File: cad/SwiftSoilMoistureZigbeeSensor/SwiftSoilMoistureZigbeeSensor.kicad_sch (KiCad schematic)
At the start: 13 parts, among them J1 Probe, J2 BAT, J3 ARM SWD 10, Q1 BSS84, SW1 Factory Reset, U1 TPS61221DCK, U2 E73-2G4M08S1C

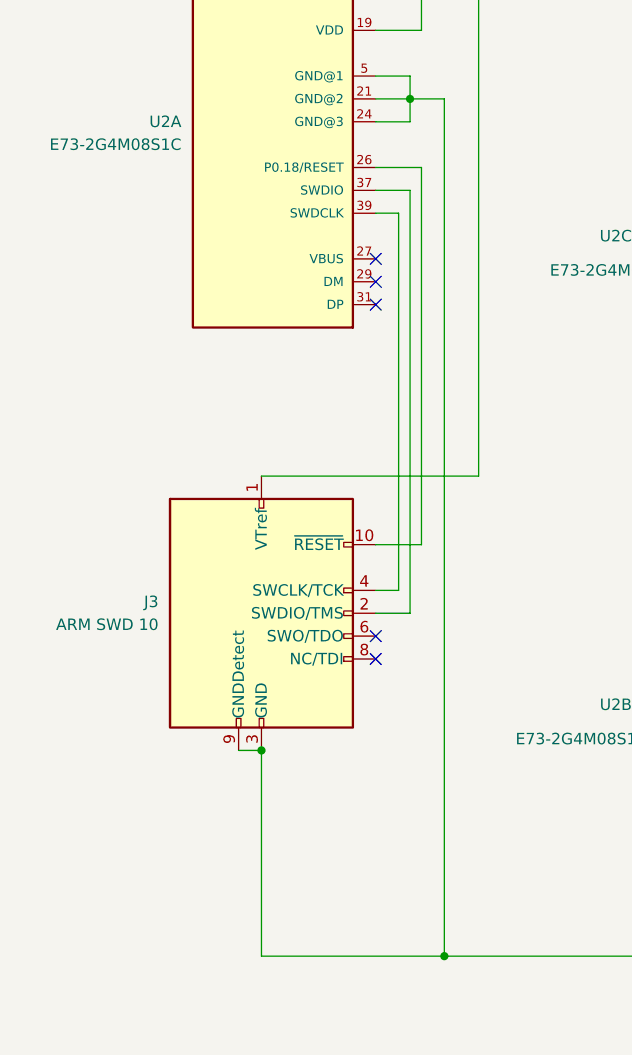
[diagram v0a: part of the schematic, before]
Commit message: Changed SWD connector
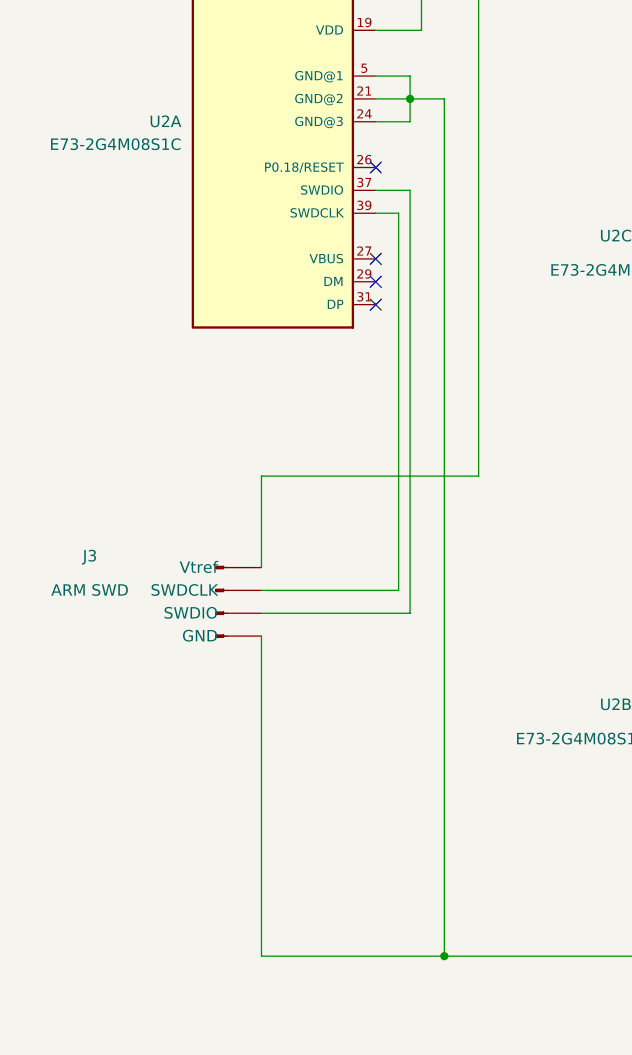
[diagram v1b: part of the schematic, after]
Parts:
- J3: value ARM SWD 10 -> ARM SWD; footprint Connector_PinHeader_1.27mm:PinHeader_2x05_P1.27mm_Vertical_SMD -> Connector_PinHeader_2.54mm:PinHeader_1x04_P2.54mm_Vertical; symbol Connector:Conn_ARM_JTAG_SWD_10 -> Connector:Conn_01x04_Pin; LCSC C2932107 -> (none)
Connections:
- net GND: now also J3.4 (GND); no longer J3.3 (GND), J3.5 (GND), J3.9 (GNDDetect)
- net at U2.26 (P0.18/RESET): no longer J3.10 (~{RESET})
- net at U2.37 (SWDIO): now also J3.3 (SWDIO); no longer J3.2 (SWDIO/TMS)
- net at U2.39 (SWDCLK): now also J3.2 (SWDCLK); no longer J3.4 (SWCLK/TCK)
- no-connect marks 32 -> 31
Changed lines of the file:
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@@
   (junction (at 171.45 60.96) (diameter 0) (color 0 0 0 0)
-  )
-  (junction (at 52.07 120.65) (diameter 0) (color 0 0 0 0)
   )
   (junction (at 130.81 143.51) (diameter 0) (color 0 0 0 0)
@@
   (no_connect (at 64.77 35.56))
   (no_connect (at 114.3 116.84))
+  (no_connect (at 64.77 55.88))
   (no_connect (at 114.3 81.28))
-  (no_connect (at 64.77 110.49))
   (no_connect (at 114.3 104.14))
   (no_connect (at 114.3 132.08))
@@
   (no_connect (at 114.3 96.52))
   (no_connect (at 114.3 57.15))
-  (no_connect (at 64.77 107.95))
   (no_connect (at 114.3 64.77))
   (no_connect (at 114.3 114.3))
@@
   (no_connect (at 114.3 99.06))
   (no_connect (at 114.3 134.62))
-  (wire (pts (xy 52.07 120.65) (xy 49.53 120.65))
-    (stroke (width 0) (type default))
-  )
   (wire (pts (xy 72.39 48.26) (xy 72.39 143.51))
     (stroke (width 0) (type default))
@@
     (stroke (width 0) (type default))
   )
-  (wire (pts (xy 64.77 102.87) (xy 67.31 102.87))
-    (stroke (width 0) (type default))
-  )
   (wire (pts (xy 114.3 88.9) (xy 179.07 88.9))
     (stroke (width 0) (type default))
@@
     (stroke (width 0) (type default))
   )
-  (wire (pts (xy 64.77 105.41) (xy 68.58 105.41))
+  (wire (pts (xy 52.07 105.41) (xy 68.58 105.41))
     (stroke (width 0) (type default))
   )
@@
     (stroke (width 0) (type default))
   )
-  (wire (pts (xy 69.85 55.88) (xy 69.85 97.79))
-    (stroke (width 0) (type default))
-  )
   (wire (pts (xy 179.07 49.53) (xy 181.61 49.53))
     (stroke (width 0) (type default))
   )
-  (wire (pts (xy 52.07 120.65) (xy 52.07 143.51))
-    (stroke (width 0) (type default))
-  )
   (wire (pts (xy 171.45 49.53) (xy 171.45 52.07))
     (stroke (width 0) (type default))
   )
+  (wire (pts (xy 52.07 102.87) (xy 67.31 102.87))
+    (stroke (width 0) (type default))
+  )
   (wire (pts (xy 227.33 88.9) (xy 241.3 88.9))
     (stroke (width 0) (type default))
@@
     (stroke (width 0) (type default))
   )
-  (wire (pts (xy 69.85 55.88) (xy 64.77 55.88))
-    (stroke (width 0) (type default))
-  )
   (wire (pts (xy 64.77 40.64) (xy 69.85 40.64))
     (stroke (width 0) (type default))
@@
     (stroke (width 0) (type default))
   )
+  (wire (pts (xy 52.07 107.95) (xy 52.07 143.51))
+    (stroke (width 0) (type default))
+  )
   (wire (pts (xy 68.58 48.26) (xy 72.39 48.26))
     (stroke (width 0) (type default))
@@
     (stroke (width 0) (type default))
   )
+  (wire (pts (xy 52.07 90.17) (xy 52.07 100.33))
+    (stroke (width 0) (type default))
+  )
   (wire (pts (xy 64.77 50.8) (xy 68.58 50.8))
     (stroke (width 0) (type default))
@@
   )
   (wire (pts (xy 179.07 52.07) (xy 179.07 88.9))
-    (stroke (width 0) (type default))
-  )
-  (wire (pts (xy 64.77 97.79) (xy 69.85 97.79))
     (stroke (width 0) (type default))
   )
@@
     )
   )
-  (symbol (lib_id "Connector:Conn_ARM_JTAG_SWD_10") (at 52.07 105.41 0) (unit 1)
-    (in_bom yes) (on_board yes) (dnp no) (fields_autoplaced)
-    (property "Reference" "J3" (at 40.64 104.14 0)
-      (effects (font (size 1.27 1.27)) (justify right))
-    )
-    (property "Value" "ARM SWD 10" (at 40.64 106.68 0)
-      (effects (font (size 1.27 1.27)) (justify right))
-    )
-    (property "Footprint" "Connector_PinHeader_1.27mm:PinHeader_2x05_P1.27mm_Vertical_SMD" (at 52.07 105.41 0)
-      (effects (font (size 1.27 1.27)) hide)
-    )
-    (property "Datasheet" "http://infocenter.arm.com/help/topic/com.arm.doc.ddi0314h/DDI0314H_coresight_components_trm.pdf" (at 43.18 137.16 90)
-      (effects (font (size 1.27 1.27)) hide)
-    )
-    (property "LCSC" "C2932107" (at 52.07 105.41 0)
-      (effects (font (size 1.27 1.27)) hide)
-    )
-    (pin "5")
+  (symbol (lib_id "Connector:Conn_01x04_Pin") (at 46.99 102.87 0) (unit 1)
+    (in_bom yes) (on_board yes) (dnp no)
+    (property "Reference" "J3" (at 33.02 99.06 0)
+      (effects (font (size 1.27 1.27)))
+    )
+    (property "Value" "ARM SWD" (at 33.02 102.87 0)
+      (effects (font (size 1.27 1.27)))
+    )
+    (property "Footprint" "Connector_PinHeader_2.54mm:PinHeader_1x04_P2.54mm_Vertical" (at 46.99 96.52 0)
+      (effects (font (size 1.27 1.27)) hide)
+    )
+    (property "Datasheet" "~" (at 46.99 102.87 0)
+      (effects (font (size 1.27 1.27)) hide)
+    )
+    (property "LCSC" "" (at 46.99 102.87 0)
+      (effects (font (size 1.27 1.27)) hide)
+    )
     (pin "2")
     (pin "3")
     (pin "4")
-    (pin "6")
-    (pin "10")
-    (pin "1")
-    (pin "7")
-    (pin "9")
-    (pin "8")
-    (instances
-      (project "SwiftSoilMoistureZigbeeSensor"
+    (pin "1")
+    (instances
+      (project "SwiftSoilMoistureZigbeeSensor"

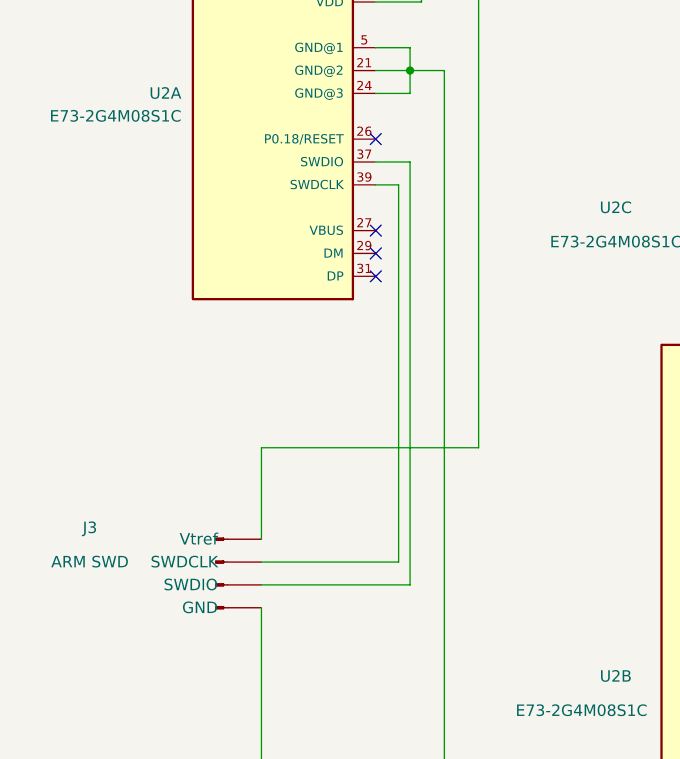
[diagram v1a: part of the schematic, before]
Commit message: Rewworked SWD connector
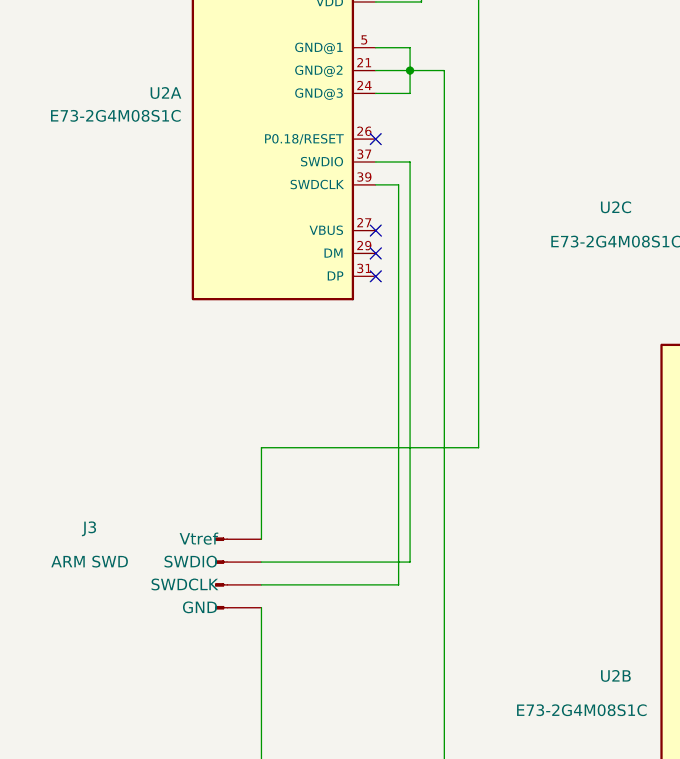
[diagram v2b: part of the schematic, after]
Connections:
- net at U2.37 (SWDIO): now also J3.2 (SWDIO); no longer J3.3 (SWDIO)
- net at U2.39 (SWDCLK): now also J3.3 (SWDCLK); no longer J3.2 (SWDCLK)
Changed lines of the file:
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@@
+    (stroke (width 0) (type default))
+  )
+  (wire (pts (xy 67.31 105.41) (xy 52.07 105.41))
     (stroke (width 0) (type default))
   )
@@
     (stroke (width 0) (type default))
   )
-  (wire (pts (xy 52.07 105.41) (xy 68.58 105.41))
+  (wire (pts (xy 196.85 60.96) (xy 208.28 60.96))
     (stroke (width 0) (type default))
   )
-  (wire (pts (xy 196.85 60.96) (xy 208.28 60.96))
+  (wire (pts (xy 52.07 102.87) (xy 68.58 102.87))
     (stroke (width 0) (type default))
   )
@@
   )
   (wire (pts (xy 171.45 49.53) (xy 171.45 52.07))
-    (stroke (width 0) (type default))
-  )
-  (wire (pts (xy 52.07 102.87) (xy 67.31 102.87))
     (stroke (width 0) (type default))
   )
@@
     (stroke (width 0) (type default))
   )
-  (wire (pts (xy 67.31 60.96) (xy 67.31 102.87))
-    (stroke (width 0) (type default))
-  )
   (wire (pts (xy 72.39 143.51) (xy 130.81 143.51))
     (stroke (width 0) (type default))
@@
   )
   (wire (pts (xy 52.07 90.17) (xy 76.2 90.17))
+    (stroke (width 0) (type default))
+  )
+  (wire (pts (xy 67.31 60.96) (xy 67.31 105.41))
     (stroke (width 0) (type default))
   )
@@
     (stroke (width 0) (type default))
   )
-  (wire (pts (xy 68.58 58.42) (xy 68.58 105.41))
+  (wire (pts (xy 68.58 58.42) (xy 68.58 102.87))
     (stroke (width 0) (type default))
   )

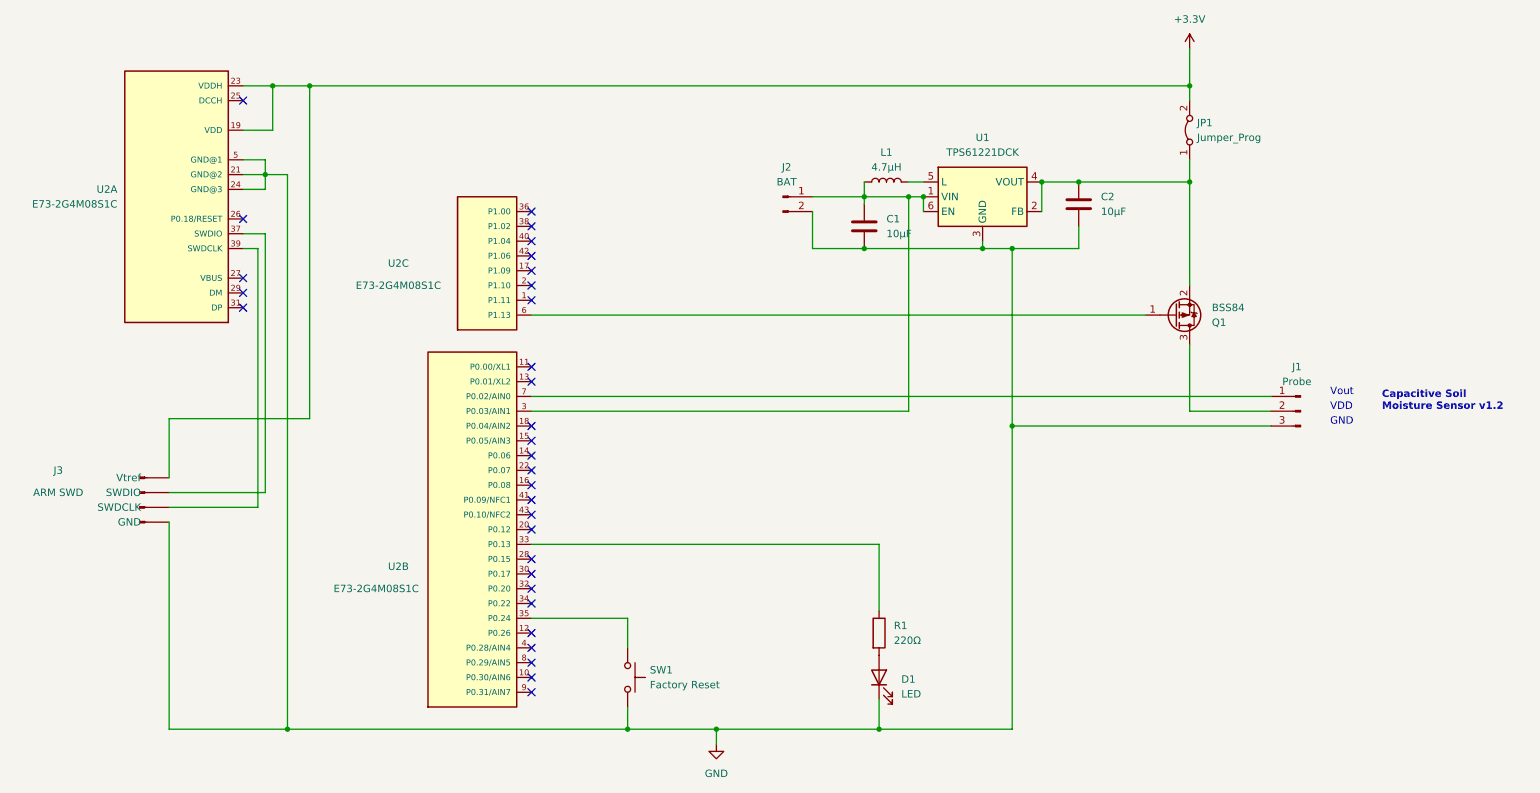
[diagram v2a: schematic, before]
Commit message: Bad LED wiring
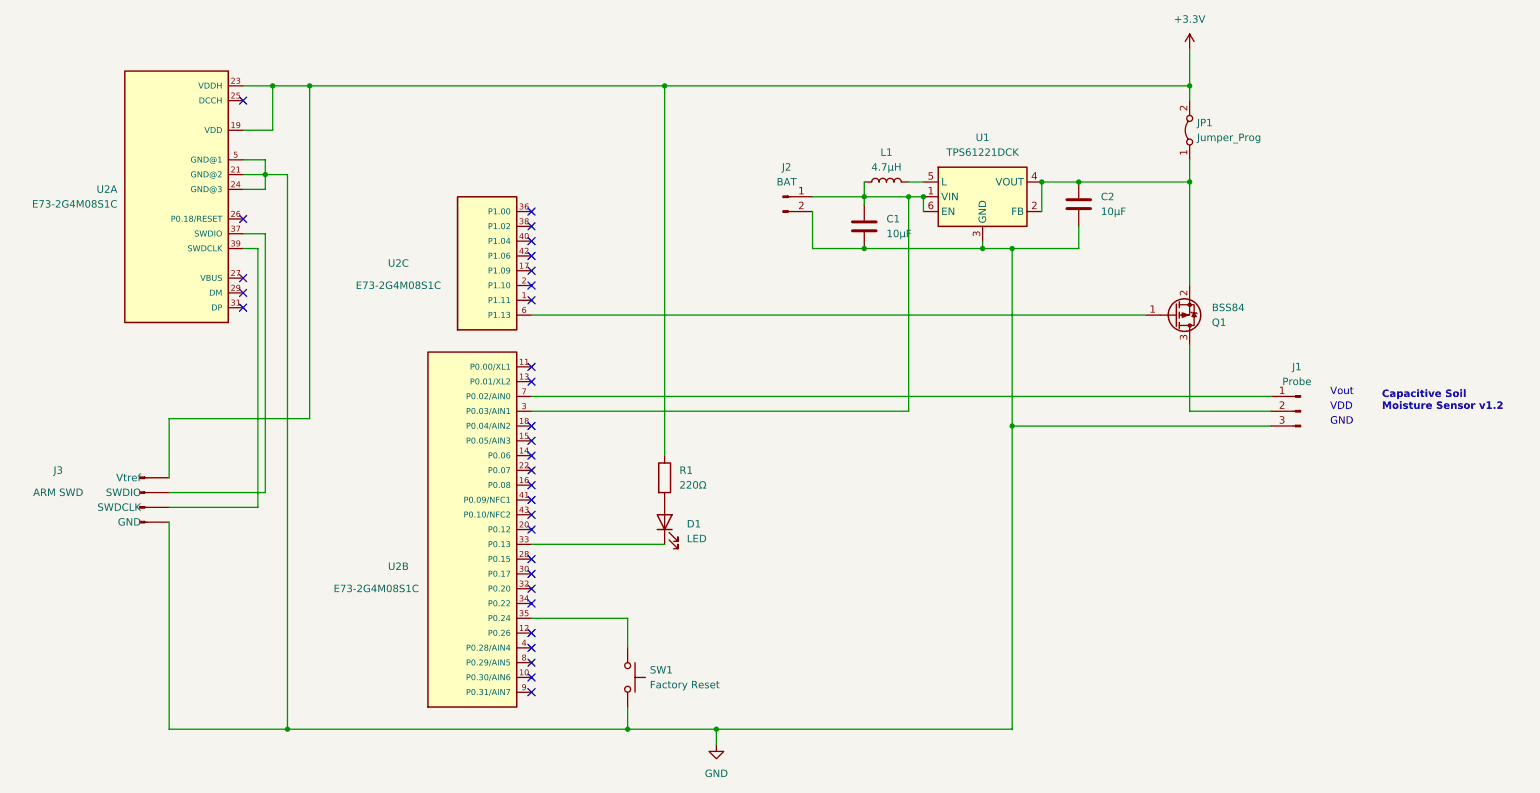
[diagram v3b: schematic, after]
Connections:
- net +3.3V: now also R1.1
- net GND: no longer D1.1 (K)
- net at U2.33 (P0.13): now also D1.1 (K); no longer R1.1
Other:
- moved on the sheet: D1, R1
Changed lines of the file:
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@@
   (title_block
     (title "Swift Zigbee Soil Moisture Sensor")
-    (date "2024-07-04")
-    (rev "1.0")
+    (date "2024-08-13")
+    (rev "1.1")
   )
   (junction (at 196.85 60.96) (diameter 0) (color 0 0 0 0)
@@
   (junction (at 208.28 49.53) (diameter 0) (color 0 0 0 0)
   )
+  (junction (at 137.16 33.02) (diameter 0) (color 0 0 0 0)
+  )
   (junction (at 179.07 52.07) (diameter 0) (color 0 0 0 0)
-  )
-  (junction (at 173.99 143.51) (diameter 0) (color 0 0 0 0)
   )
   (junction (at 191.77 60.96) (diameter 0) (color 0 0 0 0)
@@
     (stroke (width 0) (type default))
   )
-  (wire (pts (xy 173.99 138.43) (xy 173.99 143.51))
+  (wire (pts (xy 137.16 33.02) (xy 137.16 96.52))
     (stroke (width 0) (type default))
   )
@@
     (stroke (width 0) (type default))
   )
+  (wire (pts (xy 76.2 33.02) (xy 137.16 33.02))
+    (stroke (width 0) (type default))
+  )
   (wire (pts (xy 208.28 57.15) (xy 208.28 60.96))
     (stroke (width 0) (type default))
@@
     (stroke (width 0) (type default))
   )
-  (wire (pts (xy 173.99 143.51) (xy 196.85 143.51))
+  (wire (pts (xy 146.05 143.51) (xy 196.85 143.51))
     (stroke (width 0) (type default))
   )
@@
     (stroke (width 0) (type default))
   )
-  (wire (pts (xy 146.05 143.51) (xy 173.99 143.51))
-    (stroke (width 0) (type default))
-  )
   (wire (pts (xy 179.07 52.07) (xy 181.61 52.07))
     (stroke (width 0) (type default))
   )
+  (wire (pts (xy 137.16 33.02) (xy 227.33 33.02))
+    (stroke (width 0) (type default))
+  )
   (wire (pts (xy 72.39 143.51) (xy 130.81 143.51))
     (stroke (width 0) (type default))
@@
     (stroke (width 0) (type default))
   )
-  (wire (pts (xy 173.99 111.76) (xy 114.3 111.76))
+  (wire (pts (xy 137.16 111.76) (xy 114.3 111.76))
     (stroke (width 0) (type default))
   )
@@
     (stroke (width 0) (type default))
   )
-  (wire (pts (xy 173.99 123.19) (xy 173.99 111.76))
-    (stroke (width 0) (type default))
-  )
   (wire (pts (xy 52.07 143.51) (xy 72.39 143.51))
     (stroke (width 0) (type default))
@@
   )
   (wire (pts (xy 68.58 48.26) (xy 72.39 48.26))
-    (stroke (width 0) (type default))
-  )
-  (wire (pts (xy 76.2 33.02) (xy 227.33 33.02))
     (stroke (width 0) (type default))
   )
@@
     )
   )
-  (symbol (lib_id "Device:R") (at 173.99 127 0) (unit 1)
+  (symbol (lib_id "Device:R") (at 137.16 100.33 0) (unit 1)
     (in_bom yes) (on_board yes) (dnp no) (fields_autoplaced)
-    (property "Reference" "R1" (at 176.53 125.73 0)
+    (property "Reference" "R1" (at 139.7 99.06 0)
       (effects (font (size 1.27 1.27)) (justify left))
     )
-    (property "Value" "220Ω" (at 176.53 128.27 0)
+    (property "Value" "220Ω" (at 139.7 101.6 0)
       (effects (font (size 1.27 1.27)) (justify left))
     )
-    (property "Footprint" "Resistor_SMD:R_0603_1608Metric" (at 172.212 127 90)
-      (effects (font (size 1.27 1.27)) hide)
-    )
-    (property "Datasheet" "~" (at 173.99 127 0)
-      (effects (font (size 1.27 1.27)) hide)
-    )
-    (property "LCSC" "C445820" (at 173.99 127 0)
+    (property "Footprint" "Resistor_SMD:R_0603_1608Metric" (at 135.382 100.33 90)
+      (effects (font (size 1.27 1.27)) hide)
+    )
+    (property "Datasheet" "~" (at 137.16 100.33 0)
+      (effects (font (size 1.27 1.27)) hide)
+    )
+    (property "LCSC" "C445820" (at 137.16 100.33 0)
       (effects (font (size 1.27 1.27)) hide)
     )
@@
     )
   )
-  (symbol (lib_id "Device:LED") (at 173.99 134.62 90) (unit 1)
-    (in_bom yes) (on_board yes) (dnp no) (fields_autoplaced)
-    (property "Reference" "D1" (at 177.8 134.9375 90)
+  (symbol (lib_id "Device:LED") (at 137.16 107.95 90) (unit 1)
+    (in_bom yes) (on_board yes) (dnp no)
+    (property "Reference" "D1" (at 140.97 108.2675 90)
       (effects (font (size 1.27 1.27)) (justify right))
     )
-    (property "Value" "LED" (at 177.8 137.4775 90)
+    (property "Value" "LED" (at 140.97 110.8075 90)
       (effects (font (size 1.27 1.27)) (justify right))
     )
-    (property "Footprint" "LED_SMD:LED_0603_1608Metric" (at 173.99 134.62 0)
-      (effects (font (size 1.27 1.27)) hide)
-    )
-    (property "Datasheet" "~" (at 173.99 134.62 0)
-      (effects (font (size 1.27 1.27)) hide)
-    )
-    (property "LCSC" "C5246833" (at 173.99 134.62 0)
-      (effects (font (size 1.27 1.27)) hide)
-    )
+    (property "Footprint" "LED_SMD:LED_0603_1608Metric" (at 137.16 107.95 0)
+      (effects (font (size 1.27 1.27)) hide)
+    )
+    (property "Datasheet" "~" (at 137.16 107.95 0)
+      (effects (font (size 1.27 1.27)) hide)
+    )
+    (property "LCSC" "C5246833" (at 137.16 107.95 0)
+      (effects (font (size 1.27 1.27)) hide)
+    )
